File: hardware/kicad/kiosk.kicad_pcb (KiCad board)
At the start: 2 copper layers, 158 x 121 mm, 20 parts, among them J10 TerminalBlock_MaiXu_MX126-5.0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, J11 TerminalBlock_MaiXu_MX126-5.0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, J13 PinHeader_1x09_P2.54mm_Vertic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, J14 PinHeader_1x04_P2.54mm_Vertic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, J3 PinSocket_1x14_P2.54mm_Vertic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, J4 PinSocket_1x06_P2.54mm_Vertic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, J5 PinSocket_1x04_P2.54mm_Vertic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, J6 PinSocket_1x06_P2.54mm_Vertic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, J7 PinSocket_1x07_P2.54mm_Vertic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, J9 PinHeader_1x03_P2.54mm_Vertic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, U1 ESP32-S3-CAM

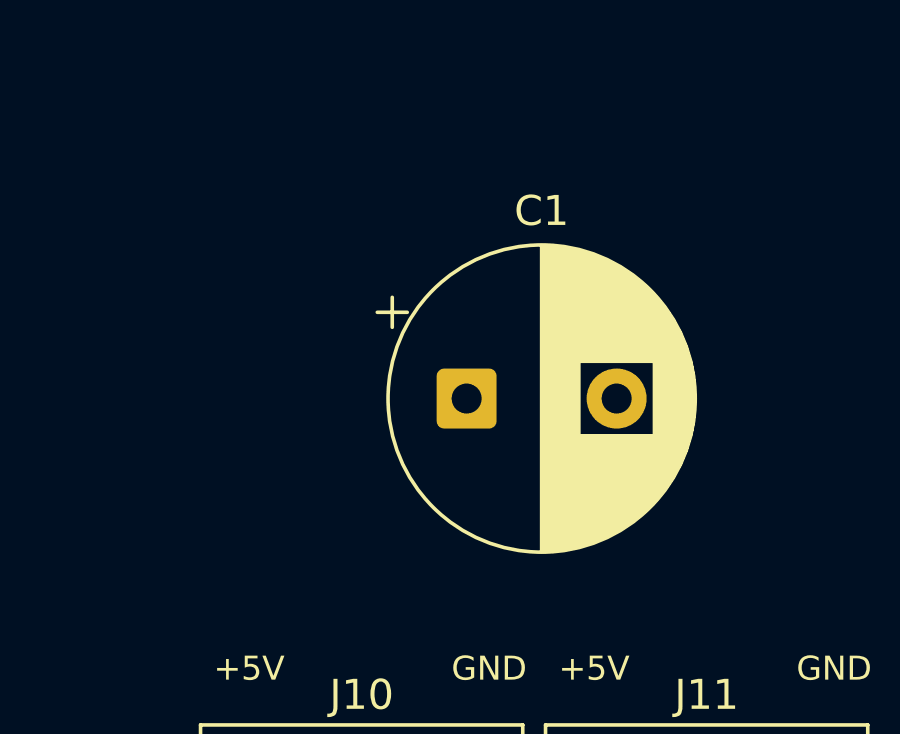
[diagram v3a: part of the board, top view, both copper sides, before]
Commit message: fix(hardware): put C1 back over the terminal whose rail it belongs to
Centring it across both terminals was wrong for a reason stronger than
looks: C1 carries +5V_R1, and J11 is +5V_R2. The two share no net, so a
capacitor drawn midway between them suggests a connection that does not
exist, and spends copper getting further from the one terminal it does
serve.

Both legs sit back on J10's, 15 mm of straight run each. Rail 2 has no
bulk store at its terminal on purpose — its 470 uF is at the servo, which
is rule 3 of section 2.5.

The terminals keep the 5.0 / 6.5 / 5.0 spacing from the last commit; that
part was not the problem.

Task: E14-T8
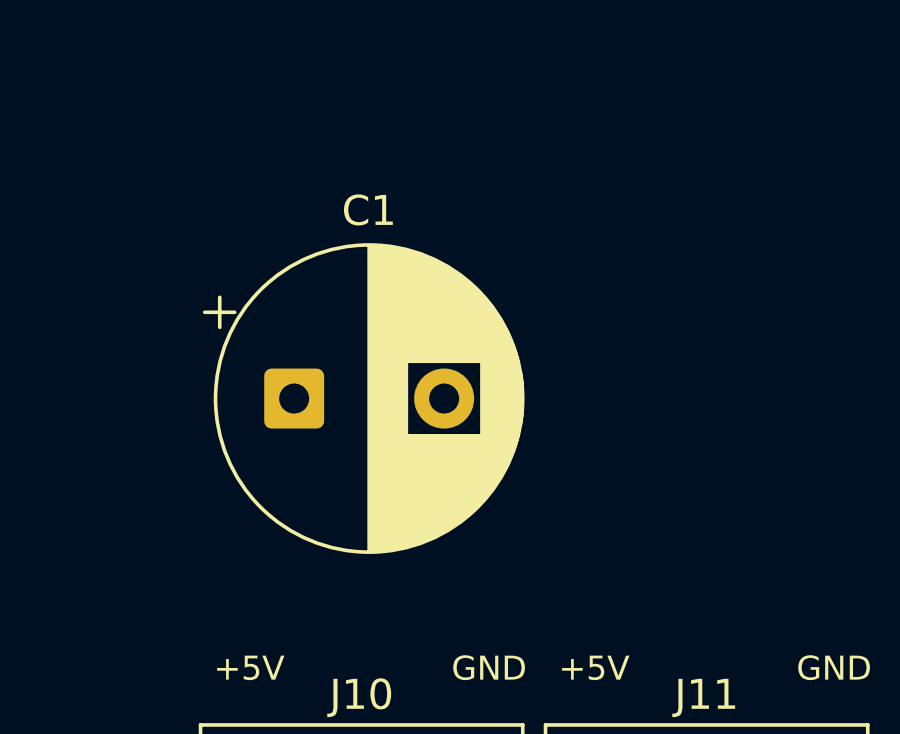
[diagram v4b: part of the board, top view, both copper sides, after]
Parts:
- moved C1 5.75 mm to (134.0, 94.0)
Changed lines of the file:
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@@
 	(footprint "Capacitor_THT:CP_Radial_D10.0mm_P5.00mm"
 		(layer "F.Cu")
-		(at 139.75 94)
+		(at 134 94)
 		(descr "CP, Radial series, Radial, pin pitch=5.00mm, diameter=10mm, height=16mm, Electrolytic Capacitor")
 		(tags "CP Radial series Radial pin pitch 5.00mm diameter 10mm height 16mm Electrolytic Capacitor")

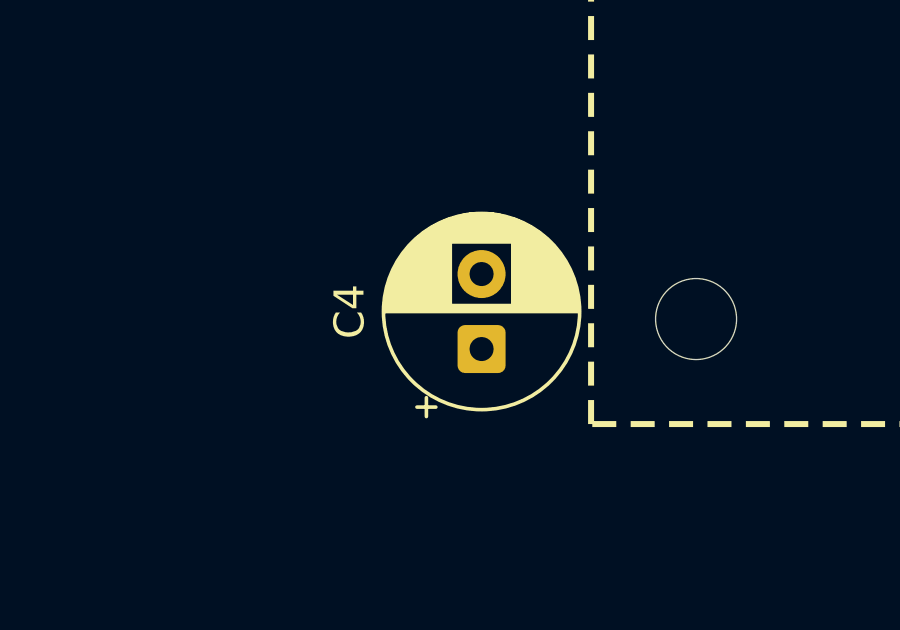
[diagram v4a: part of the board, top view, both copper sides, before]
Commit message: fix(hardware): specify a 5 mm can for the panel's capacitor
C4 had 0.25 mm of courtyard either side — the tightest clearance on the
board, and it is there because a 6.8 mm outline was put in a 7.30 mm gap.
The gap cannot grow: it is fixed at 7.30 by balancing it against the two
on the other side of the panel, and those are bounded by the board edge on
one end and the devkit's pin names on the other.

So the can shrinks instead. A 100 uF in a 5 mm body is an ordinary part,
and the 5.0 and 6.3 mm packages share the same 2.50 mm lead pitch, so not
a single drill moves — the change is a specification of what to buy, not a
layout change. Clearance goes to 0.90 mm a side.

Buying the 6.3 mm can by mistake still fits the holes. It just sits where
it sat before this commit.

Task: E14-T8
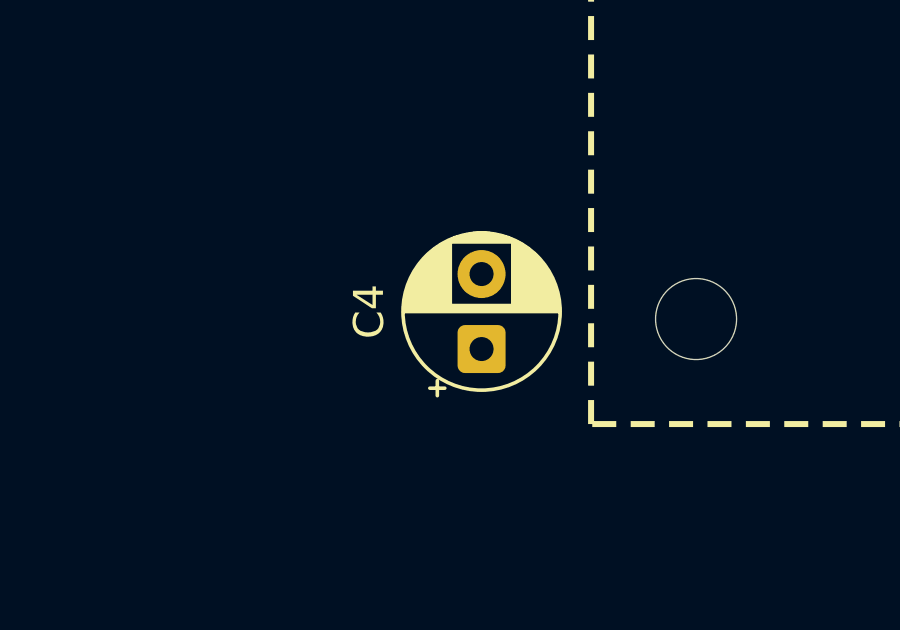
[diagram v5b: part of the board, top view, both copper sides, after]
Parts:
- C4: value CP_Radial_D6.3mm_P2.50mm -> CP_Radial_D5.0mm_P2.50mm; footprint Capacitor_THT:CP_Radial_D6.3mm_P2.50mm -> Capacitor_THT:CP_Radial_D5.0mm_P2.50mm

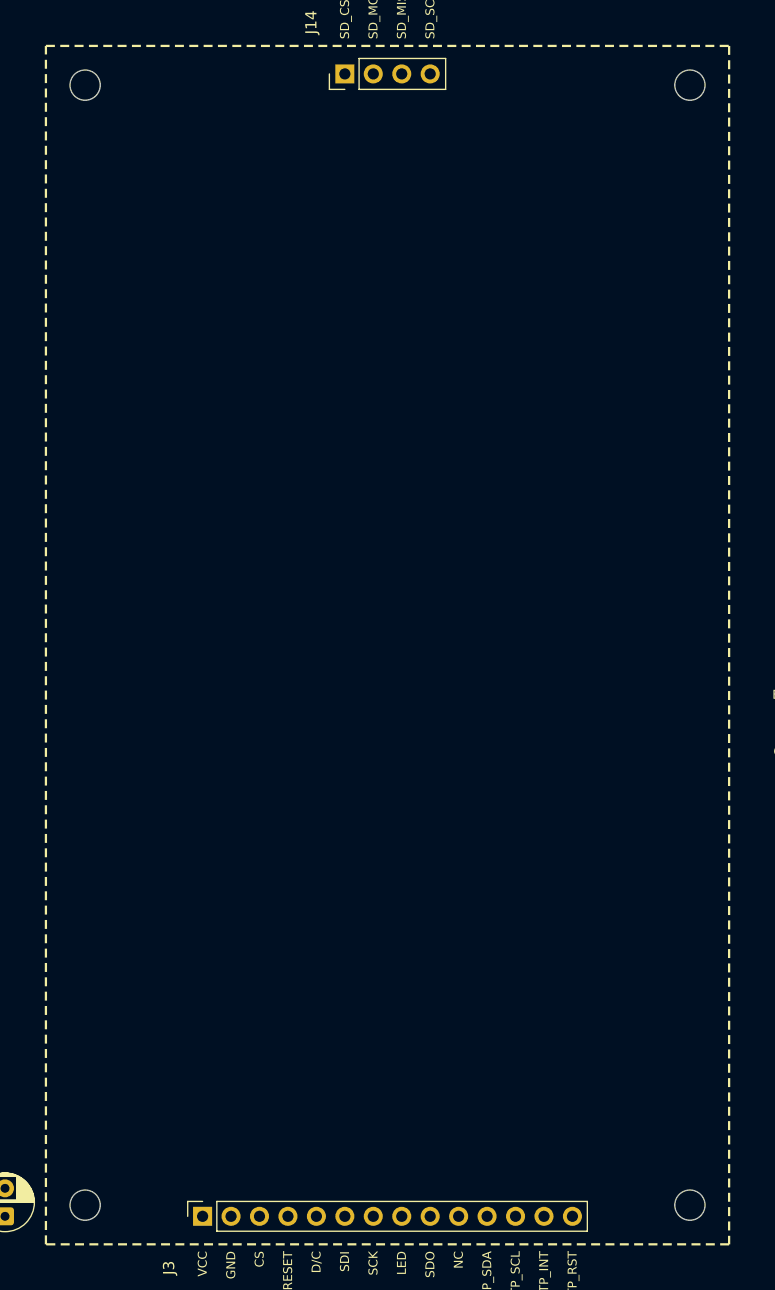
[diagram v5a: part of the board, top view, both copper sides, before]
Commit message: fix(hardware): drill the panel's mounting holes for M3, not M2.5
The panel's own holes measure 3.5 mm, which is an M3 clearance hole — the
module is built for M3 and nothing else. The carrier was drilled 2.7 for
M2.5, so the two would have taken different screws through the same
standoff.

Carrier holes go to 3.2 mm. An M3 through 3.5 and then 3.2 can shift
0.35 mm total, which is the whole tolerance budget for hole positions that
are still unmeasured — the answer to that is the measurement, not a
sloppier screw.

The standoff note was also wrong in one direction. A post shorter than the
8.5 mm the socket holds the panel at is harmless: the screws pull the panel
down and the pins seat deeper. A taller one is the failure, because the
panel then rests on the post with its pins short of home. So the rule is
"never taller than 8.5", and the length to buy is 8 mm, which is stocked;
8.5 is not.

Task: E14-T8
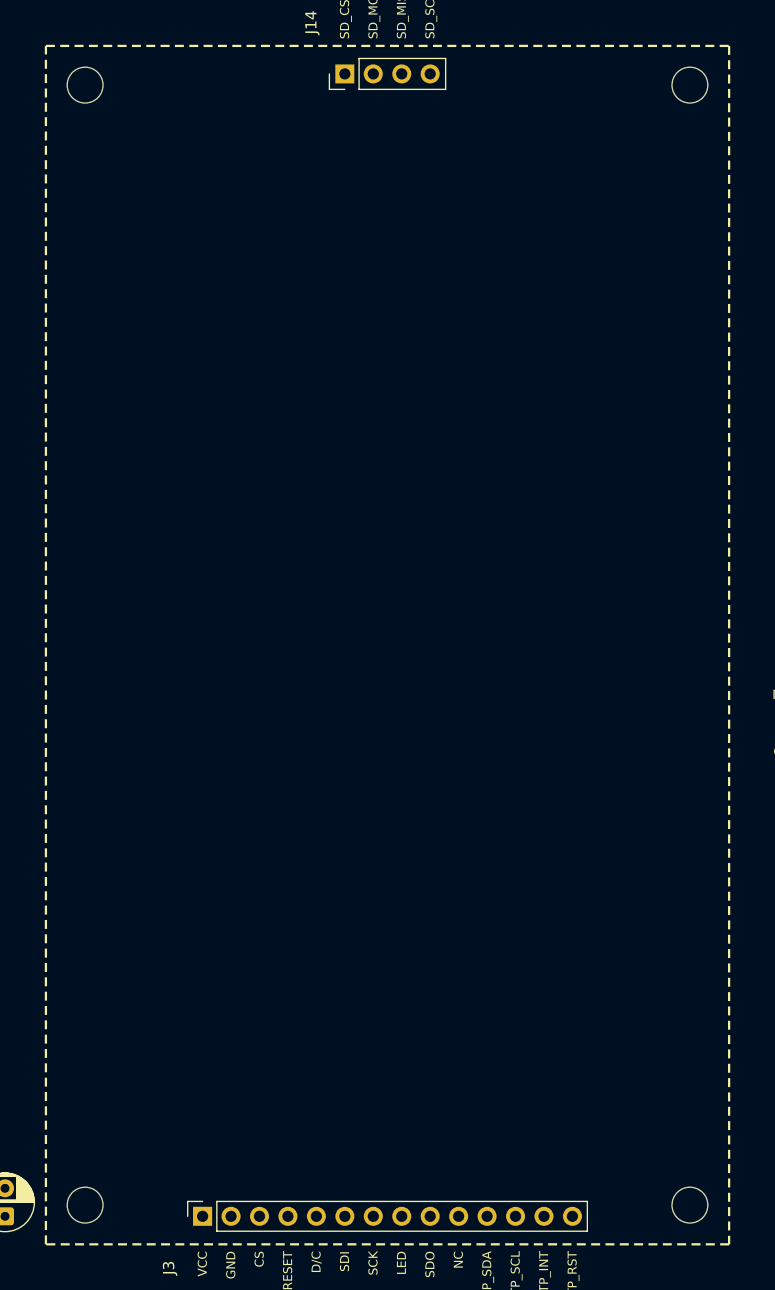
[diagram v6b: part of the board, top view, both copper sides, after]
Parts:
- H1, H2, H3, H4: value MountingHole_2.7mm -> MountingHole_3.2mm_M3; footprint MountingHole:MountingHole_2.7mm -> MountingHole:MountingHole_3.2mm_M3
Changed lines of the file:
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@@
 		)
 	)
-	(footprint "MountingHole:MountingHole_2.7mm"
+	(footprint "MountingHole:MountingHole_3.2mm_M3"
 		(layer "F.Cu")
 		(at 99.05 10.5)
-		(descr "Mounting Hole 2.7mm, no annular, generated by kicad-footprint-generator mountinghole.py")
-		(tags "mountinghole")
+		(descr "Mounting Hole 3.2mm, M3, no annular, generated by kicad-footprint-generator mountinghole.py")
+		(tags "mountinghole M3")
 		(property "Reference" "H2"
-			(at 0 -3.65 0)
+			(at 0 -4.15 0)
 			(layer "F.SilkS")
 			(hide yes)
@@
 			)
 		)
-		(property "Value" "MountingHole_2.7mm"
-			(at 0 3.65 0)
+		(property "Value" "MountingHole_3.2mm_M3"
+			(at 0 4.15 0)
 			(layer "F.Fab")
 			(effects
@@
 		(fp_circle
 			(center 0 0)
-			(end 2.7 0)
+			(end 3.2 0)
 			(stroke
 				(width 0.15)
@@
 		(fp_circle
 			(center 0 0)
-			(end 2.95 0)
+			(end 3.45 0)
 			(stroke
 				(width 0.05)
@@
 		(pad "" np_thru_hole circle
 			(at 0 0)
-			(size 2.7 2.7)
-			(drill 2.7)
+			(size 3.2 3.2)
+			(drill 3.2)
 			(layers "*.Cu" "*.Mask")
 		)
@@
 		)
 	)
-	(footprint "MountingHole:MountingHole_2.7mm"
+	(footprint "MountingHole:MountingHole_3.2mm_M3"
 		(layer "F.Cu")
 		(at 45.05 110.5)
-		(descr "Mounting Hole 2.7mm, no annular, generated by kicad-footprint-generator mountinghole.py")
-		(tags "mountinghole")
+		(descr "Mounting Hole 3.2mm, M3, no annular, generated by kicad-footprint-generator mountinghole.py")
+		(tags "mountinghole M3")
 		(property "Reference" "H4"
-			(at 0 -3.65 0)
+			(at 0 -4.15 0)
 			(layer "F.SilkS")
 			(hide yes)
@@
 			)
 		)
-		(property "Value" "MountingHole_2.7mm"
-			(at 0 3.65 0)
+		(property "Value" "MountingHole_3.2mm_M3"
+			(at 0 4.15 0)
 			(layer "F.Fab")
 			(effects
@@
 		(fp_circle
 			(center 0 0)
-			(end 2.7 0)
+			(end 3.2 0)
 			(stroke
 				(width 0.15)
@@
 		(fp_circle
 			(center 0 0)
-			(end 2.95 0)
+			(end 3.45 0)
 			(stroke
 				(width 0.05)
@@
 		(pad "" np_thru_hole circle
 			(at 0 0)
-			(size 2.7 2.7)
-			(drill 2.7)
+			(size 3.2 3.2)
+			(drill 3.2)
 			(layers "*.Cu" "*.Mask")
 		)
@@
 		)
 	)
-	(footprint "MountingHole:MountingHole_2.7mm"
+	(footprint "MountingHole:MountingHole_3.2mm_M3"
 		(layer "F.Cu")
 		(at 99.05 110.5)
-		(descr "Mounting Hole 2.7mm, no annular, generated by kicad-footprint-generator mountinghole.py")
-		(tags "mountinghole")
+		(descr "Mounting Hole 3.2mm, M3, no annular, generated by kicad-footprint-generator mountinghole.py")
+		(tags "mountinghole M3")
 		(property "Reference" "H3"
-			(at 0 -3.65 0)
+			(at 0 -4.15 0)
 			(layer "F.SilkS")
 			(hide yes)
@@
 			)
 		)
-		(property "Value" "MountingHole_2.7mm"
-			(at 0 3.65 0)
+		(property "Value" "MountingHole_3.2mm_M3"
+			(at 0 4.15 0)
 			(layer "F.Fab")
 			(effects
@@
 		(fp_circle
 			(center 0 0)
-			(end 2.7 0)
+			(end 3.2 0)
 			(stroke
 				(width 0.15)
@@
 		(fp_circle
 			(center 0 0)
-			(end 2.95 0)
+			(end 3.45 0)
 			(stroke
 				(width 0.05)
@@
 		(pad "" np_thru_hole circle
 			(at 0 0)
-			(size 2.7 2.7)
-			(drill 2.7)
+			(size 3.2 3.2)
+			(drill 3.2)
 			(layers "*.Cu" "*.Mask")
 		)
 		(embedded_fonts no)
 	)
-	(footprint "MountingHole:MountingHole_2.7mm"
+	(footprint "MountingHole:MountingHole_3.2mm_M3"
 		(layer "F.Cu")
 		(at 45.05 10.5)
-		(descr "Mounting Hole 2.7mm, no annular, generated by kicad-footprint-generator mountinghole.py")
-		(tags "mountinghole")
+		(descr "Mounting Hole 3.2mm, M3, no annular, generated by kicad-footprint-generator mountinghole.py")
+		(tags "mountinghole M3")
 		(property "Reference" "H1"
-			(at 0 -3.65 0)
+			(at 0 -4.15 0)
 			(layer "F.SilkS")
 			(hide yes)
@@
 			)
 		)
-		(property "Value" "MountingHole_2.7mm"
-			(at 0 3.65 0)
+		(property "Value" "MountingHole_3.2mm_M3"
+			(at 0 4.15 0)
 			(layer "F.Fab")
 			(effects
@@
 		(fp_circle
 			(center 0 0)
-			(end 2.7 0)
+			(end 3.2 0)
 			(stroke
 				(width 0.15)
@@
 		(fp_circle
 			(center 0 0)
-			(end 2.95 0)
+			(end 3.45 0)
 			(stroke
 				(width 0.05)
@@
 		(pad "" np_thru_hole circle
 			(at 0 0)
-			(size 2.7 2.7)
-			(drill 2.7)
+			(size 3.2 3.2)
+			(drill 3.2)
 			(layers "*.Cu" "*.Mask")
 		)
